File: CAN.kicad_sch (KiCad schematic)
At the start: 12 parts, among them U4 SIT65HVD230DR

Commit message: 更新原理图
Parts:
- removed C27: 1nF, kicad_community_lib:CC1206JKX7RDBB102, symbol CC1206JKX7RDBB102:CC1206JKX7RDBB102
- removed C29, C30: 100nF, kicad_api_lib:0402B104J160CT, symbol 0402B104J160CT:0402B104J160CT
- removed D3, D4: PESD12VV1BL-N, kicad_api_lib:PESD12VV1BL-N, symbol PESD12VV1BL-N:PESD12VV1BL-N
- removed R10: 10K, kicad_api_lib:AC0603JR-0710KL, symbol AC0603JR-0710KL:AC0603JR-0710KL
- removed R11: 120, kicad_api_lib:CRCW0603120RFKEA, symbol CRCW0603120RFKEA:CRCW0603120RFKEA
- removed R12, R13: 10, kicad_api_lib:AC0402FR-0710RL, symbol AC0402FR-0710RL:AC0402FR-0710RL
- removed R8: 0, kicad_api_lib:AC0603FR-070RL, symbol AC0603FR-070RL:AC0603FR-070RL
- removed R9: 1M, kicad_community_lib:RK73B1JTTD105J, symbol RK73B1JTTD105J:RK73B1JTTD105J
- removed U4: SIT65HVD230DR, kicad_api_lib:SIT65HVD230DR, symbol SIT65HVD230DR:SIT65HVD230DR
- added C27: 100nF, kicad_api_lib:CL05B104KB54PNC, symbol CL05B104KB54PNC:CL05B104KB54PNC
- added CN1: PZ254-1-02-W-8.5, kicad_api_lib:PZ254-1-02-W-8.5, symbol PZ254-1-02-W-8.5:FWF12507-S02B24W5B
- added D3: ESDA6V1L, kicad_api_lib:ESDA6V1L, symbol ESDA6V1L:ESDA6V1L
- added R9: 120, kicad_api_lib:0603WAF1200T5E, symbol 0603WAF1200T5E:0603WAF1200T5E
- added U4: ISO1050DWR, kicad_api_lib:ISO1050DWR, symbol ISO1050DWR:ISO1050DWR
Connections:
- net GND: now also C27.2, D3.3 (A), U4.10 (GND2), U4.15 (GND2), U4.2 (GND1), U4.7 (GND1), U4.8 (GND1), U4.9 (GND2)
- new net: CN1.2, R9.2
- new net +3.3V: U4.1 (VCC1)
- new net +5V: C27.1, U4.16 (VCC2)
- new net CANH: CN1.1, D3.1 (K1), U4.13 (CANH)
- new net CANL: D3.2 (K2), R9.1, U4.12 (CANL)
- new net CAN_RXD: U4.3 (RXD)
- new net CAN_TXD: U4.6 (TXD)
- no-connect marks 0 -> 4
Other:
- note added: "ISO1050DWR_Isolated CAN Transceiver Module"
- note added: "模块电路功能： 这是一个带隔离功能的 CAN 总线收发器电路，采用半双工，最高支持1Mbps CAN 通信速率； 该电路的主要功能是将微控制器的逻辑电平信号（TXD/RXD） 转换为 CAN 总线的差分信号（CANH/CANL）， 同时在逻辑侧和总线侧之间提供电气隔离。 引脚功能： MCU 的 TXD → ISO1050DWR → 驱动 CAN_H/CAN_L 差分信号上总线。 CAN_H/CAN_L 差分信号 → ISO1050DWR → 输出 RXD 给 MCU。 应用场景： 适用于PLC、伺服驱动器、工业机器人的 CAN/CANopen 通信隔离；"
- note removed: "SIT65HVD230DR_CAN Bus Transceiver Module"
- note removed: "模块电路功能： 一款 CAN 总线收发器芯片，该芯片是 CAN 协议控制器和物理总线之间的接口芯片， 可与具有 CAN 控制器的 3.3V 微处理器、微控制器（MCU）和数字信号处理器（DSP）等结合使用， 采用 3.3V 单电源供电，总线引脚 ESD 保护超过 ±15kV 人体模型（HBM）， 单电源工作电压范围为 3.0 V～3.6 V（VCC 引脚），典型工作电压为 3.3 V"

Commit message: 增加USB,TYPEC转串口esd隔离，
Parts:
- added C41: 100nF, kicad_api_lib:CL05B104KB54PNC, symbol CL05B104KB54PNC:CL05B104KB54PNC
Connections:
- net +3.3V renamed +3.3V_ISO
- net +3.3V_ISO: now also C41.1
- net +5V renamed +5V_ISO
- net GND renamed GNDS
- net GNDS: now also C41.2

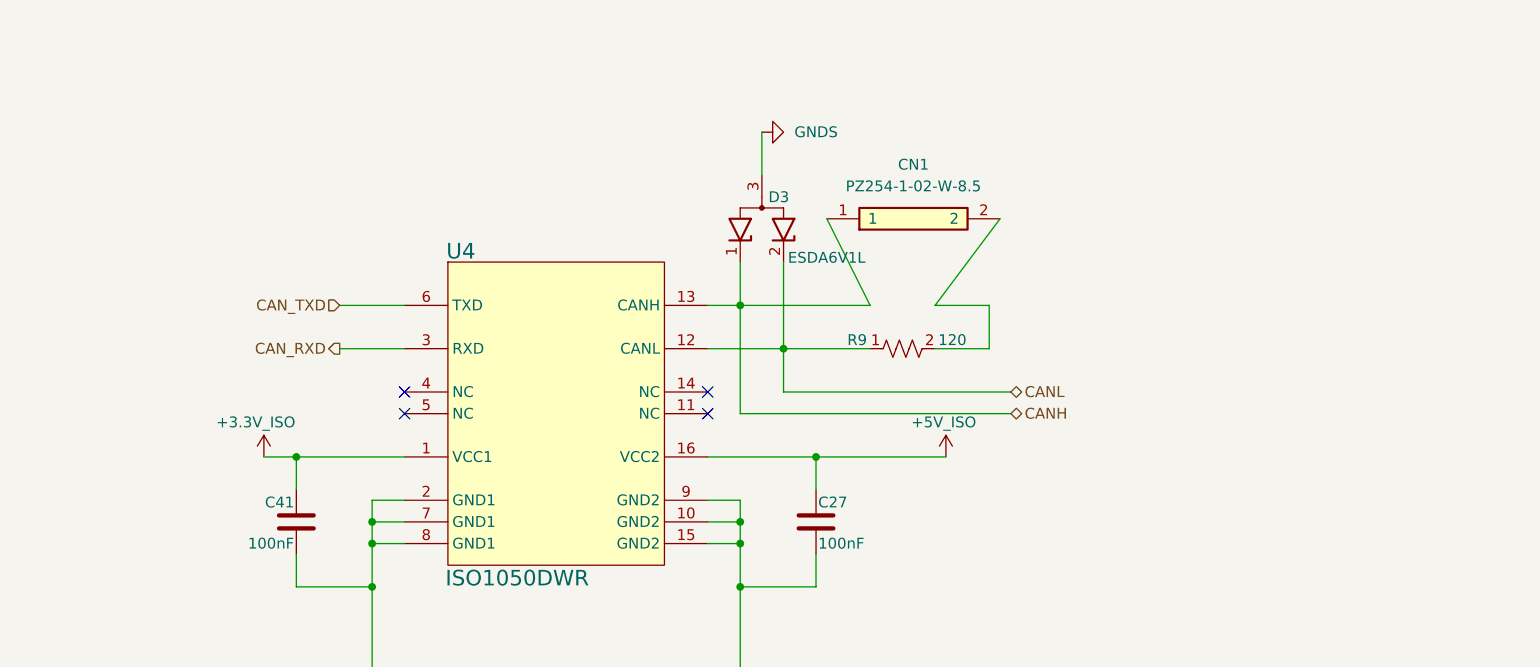
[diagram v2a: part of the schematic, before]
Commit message: 完成GD32F303控制板原理图与PCB设计
- 更新电源、CAN、RS232、RS485及电机通信子电路
- 切换并完善GD32F303VCT6核心原理图
- 新增PCB布局及所需符号、封装库文件
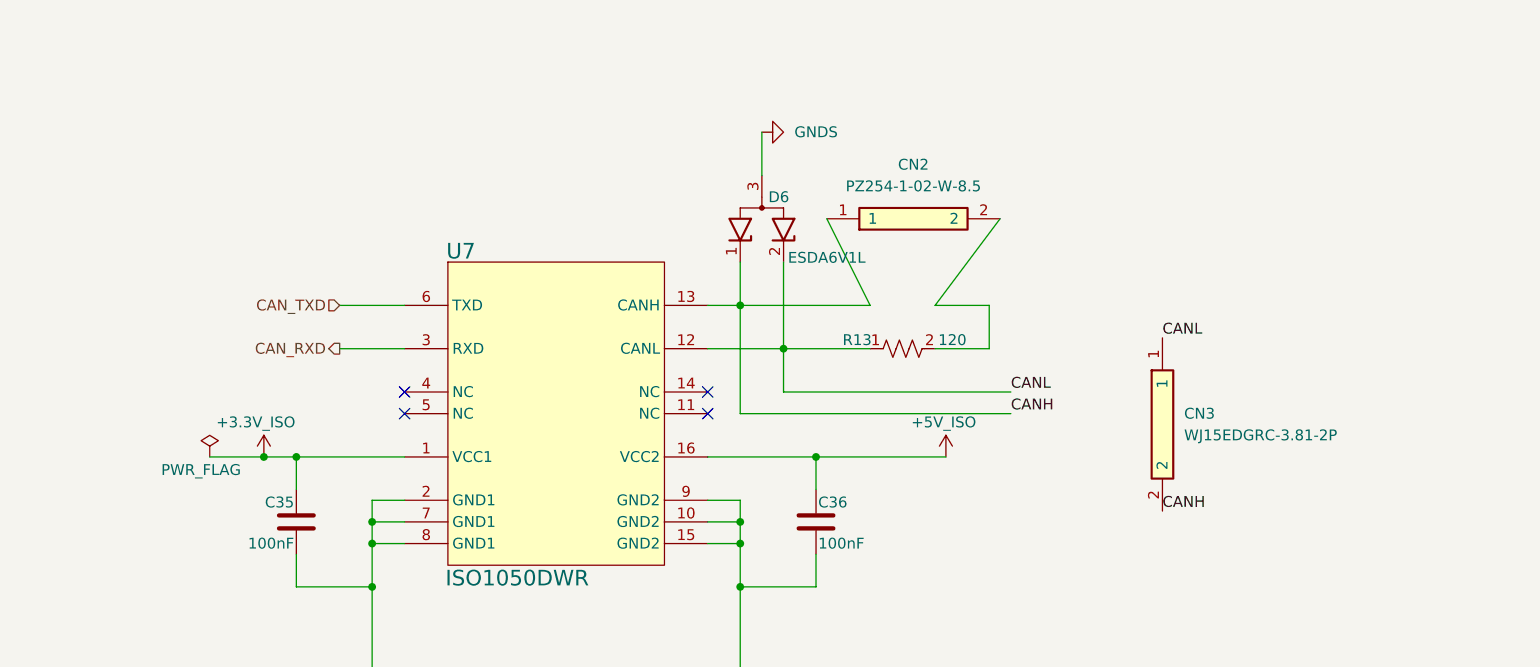
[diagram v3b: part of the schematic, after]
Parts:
- added CN3: WJ15EDGRC-3.81-2P, kicad_api_lib:WJ15EDGRC-3.81-2P, symbol WJ15EDGRC-3.81-2P:31330102
- C35: renamed from C41; footprint kicad_api_lib:CL05B104KB54PNC -> Capacitor_SMD:C_0402_1005Metric_Pad0.74x0.62mm_HandSolder
- C36: renamed from C27; footprint kicad_api_lib:CL05B104KB54PNC -> Capacitor_SMD:C_0402_1005Metric_Pad0.74x0.62mm_HandSolder
- D6: renamed from D3; footprint kicad_api_lib:ESDA6V1L -> Package_TO_SOT_SMD:SOT-23-3
- R13: renamed from R9; footprint kicad_api_lib:0603WAF1200T5E -> Resistor_SMD:R_0603_1608Metric_Pad0.98x0.95mm_HandSolder
- U7: renamed from U4; footprint kicad_api_lib:ISO1050DWR -> Package_SO:SOIC-16_3.9x9.9mm_P1.27mm
- renumbered CN1 to CN2
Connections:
- net CANH: now also CN3.2
- net CANL: now also CN3.1

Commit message: 优化接口原理图与PCB布局
- 精简CAN接口并调整各子页器件编号
- 更新电源输入端子与Type-C接口封装
- 重新整理控制板PCB器件布局
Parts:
- removed CN2: PZ254-1-02-W-8.5, kicad_api_lib:PZ254-1-02-W-8.5, symbol PZ254-1-02-W-8.5:FWF12507-S02B24W5B
- renumbered CN3 to CN2
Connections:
- net CANH: now also R13.2

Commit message: 完善PCB布线与接口电源网络
- 调整控制板PCB器件布局与走线
- 更新MCU、电源及通信接口原理图
- 统一隔离接口地和电源网络标签并修正封装属性
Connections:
- net GNDS: no longer C35.2, U7.2 (GND1), U7.7 (GND1), U7.8 (GND1)
- new net GND: C35.2, U7.2 (GND1), U7.7 (GND1), U7.8 (GND1)
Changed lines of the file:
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@@
 			)
 		)
-		(property "Value" "GNDS"
+		(property "Value" "GND"
 			(at 111.76 121.92 0)
 			(show_name no)

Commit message: 完善总线映射并划分隔离地与电源平面
统一3V3电源网络并消除ERC错误；优化GND/Earth耦合器件布局；完成In1.Cu地平面及In2.Cu电源平面分区。
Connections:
- net +3.3V_ISO renamed +3V3
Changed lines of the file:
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@@
-	)
-	(symbol
-		(lib_id "power:PWR_FLAG")
-		(at 92.71 91.44 0)
-		(unit 1)
-		(body_style 1)
-		(exclude_from_sim no)
-		(in_bom yes)
-		(on_board yes)
-		(in_pos_files yes)
-		(dnp no)
-		(property "Reference" "#FLG013"
-			(at 92.71 89.535 0)
-			(hide yes)
-			(show_name no)
-			(do_not_autoplace no)
-			(effects
-				(font
-					(size 1.27 1.27)
-				)
-			)
-		)
-		(property "Value" "PWR_FLAG"
-			(at 91.694 92.964 0)
-			(show_name no)
-			(do_not_autoplace no)
-			(effects
-				(font
-					(size 1.27 1.27)
-				)
-			)
-		)
-		(property "Footprint" ""
-			(at 92.71 91.44 0)
-			(hide yes)
-			(show_name no)
-			(do_not_autoplace no)
-			(effects
-				(font
-					(size 1.27 1.27)
-				)
-			)
-		)
-		(property "Datasheet" ""
-			(at 92.71 91.44 0)
-			(hide yes)
-			(show_name no)
-			(do_not_autoplace no)
-			(effects
-				(font
-					(size 1.27 1.27)
-				)
-			)
-		)
-		(property "Description" "Special symbol for telling ERC where power comes from"
-			(at 92.71 91.44 0)
-			(hide yes)
-			(show_name no)
-			(do_not_autoplace no)
-			(effects
-				(font
-					(size 1.27 1.27)
-				)
-			)
-		)
-		(pin "1"
-		)
-		(instances
-			(project "GD32F303"
-				(path "/54005433-e3aa-4693-8f75-bb73943288d3/46739a1c-a686-46fc-8f12-984396225a7f"
-					(reference "#FLG013")
-					(unit 1)
-				)
-			)
-		)
 	)
 	(symbol
@@
 			)
 		)
-		(property "Value" "+3.3V_ISO"
+		(property "Value" "+3V3"
 			(at 93.472 87.376 0)
 			(show_name no)

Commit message: 更新六层控制板设计及嘉立创生产文件
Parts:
- renumbered C35 to C36, C36 to C37, D6 to D8, R13 to R15
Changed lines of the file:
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@@
 		(dnp no)
 		(fields_autoplaced yes)
-		(property "Reference" "#PWR047"
+		(property "Reference" "#PWR053"
 			(at 111.76 123.19 0)
 			(hide yes)
@@
 			(project "GD32F303VET6_4Motor_Control"
 				(path "/54005433-e3aa-4693-8f75-bb73943288d3/46739a1c-a686-46fc-8f12-984396225a7f"
-					(reference "#PWR047")
+					(reference "#PWR053")
 					(unit 1)
 				)
@@
 		(in_pos_files yes)
 		(dnp no)
-		(property "Reference" "#PWR046"
+		(property "Reference" "#PWR052"
 			(at 99.06 95.25 0)
 			(hide yes)
@@
 			(project "GD32F303VET6_4Motor_Control"
 				(path "/54005433-e3aa-4693-8f75-bb73943288d3/46739a1c-a686-46fc-8f12-984396225a7f"
-					(reference "#PWR046")
+					(reference "#PWR052")
 					(unit 1)
 				)
@@
 		(in_pos_files yes)
 		(dnp no)
-		(property "Reference" "D6"
+		(property "Reference" "D8"
 			(at 158.242 60.96 0)
 			(show_name no)
@@
 			(project "GD32F303VET6_4Motor_Control"
 				(path "/54005433-e3aa-4693-8f75-bb73943288d3/46739a1c-a686-46fc-8f12-984396225a7f"
-					(reference "D6")
+					(reference "D8")
 					(unit 1)
 				)
@@
 		(dnp no)
 		(fields_autoplaced yes)
-		(property "Reference" "#PWR049"
+		(property "Reference" "#PWR055"
 			(at 163.83 53.34 0)
 			(hide yes)
@@
 			(project "GD32F303VET6_4Motor_Control"
 				(path "/54005433-e3aa-4693-8f75-bb73943288d3/46739a1c-a686-46fc-8f12-984396225a7f"
-					(reference "#PWR049")
+					(reference "#PWR055")
 					(unit 1)
 				)
@@
 		(dnp no)
 		(fields_autoplaced yes)
-		(property "Reference" "#PWR048"
+		(property "Reference" "#PWR054"
 			(at 154.94 123.19 0)
 			(hide yes)
@@
 			(project "GD32F303VET6_4Motor_Control"
 				(path "/54005433-e3aa-4693-8f75-bb73943288d3/46739a1c-a686-46fc-8f12-984396225a7f"
-					(reference "#PWR048")
+					(reference "#PWR054")
 					(unit 1)
 				)
@@
 		(in_pos_files yes)
 		(dnp no)
-		(property "Reference" "C35"
+		(property "Reference" "C36"
 			(at 102.616 96.774 0)
 			(show_name no)
@@
 			(project "GD32F303VET6_4Motor_Control"
 				(path "/54005433-e3aa-4693-8f75-bb73943288d3/46739a1c-a686-46fc-8f12-984396225a7f"
-					(reference "C35")
+					(reference "C36")
 					(unit 1)
 				)
@@
 		(in_pos_files yes)
 		(dnp no)
-		(property "Reference" "C36"
+		(property "Reference" "C37"
 			(at 164.084 96.774 0)
 			(show_name no)
@@
 			(project "GD32F303VET6_4Motor_Control"
 				(path "/54005433-e3aa-4693-8f75-bb73943288d3/46739a1c-a686-46fc-8f12-984396225a7f"
-					(reference "C36")
+					(reference "C37")
 					(unit 1)
 				)
@@
 		(in_pos_files yes)
 		(dnp no)
-		(property "Reference" "R13"
+		(property "Reference" "R15"
 			(at 168.656 77.724 90)
 			(show_name no)
@@
 			(project "GD32F303VET6_4Motor_Control"
 				(path "/54005433-e3aa-4693-8f75-bb73943288d3/46739a1c-a686-46fc-8f12-984396225a7f"
-					(reference "R13")
+					(reference "R15")
 					(unit 1)
 				)
@@
 		(in_pos_files yes)
 		(dnp no)
-		(property "Reference" "#PWR050"
+		(property "Reference" "#PWR056"
 			(at 179.07 95.25 0)
 			(hide yes)
@@
 			(project "GD32F303VET6_4Motor_Control"
 				(path "/54005433-e3aa-4693-8f75-bb73943288d3/46739a1c-a686-46fc-8f12-984396225a7f"
-					(reference "#PWR050")
+					(reference "#PWR056")
 					(unit 1)
 				)
